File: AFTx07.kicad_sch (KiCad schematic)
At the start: 1 part

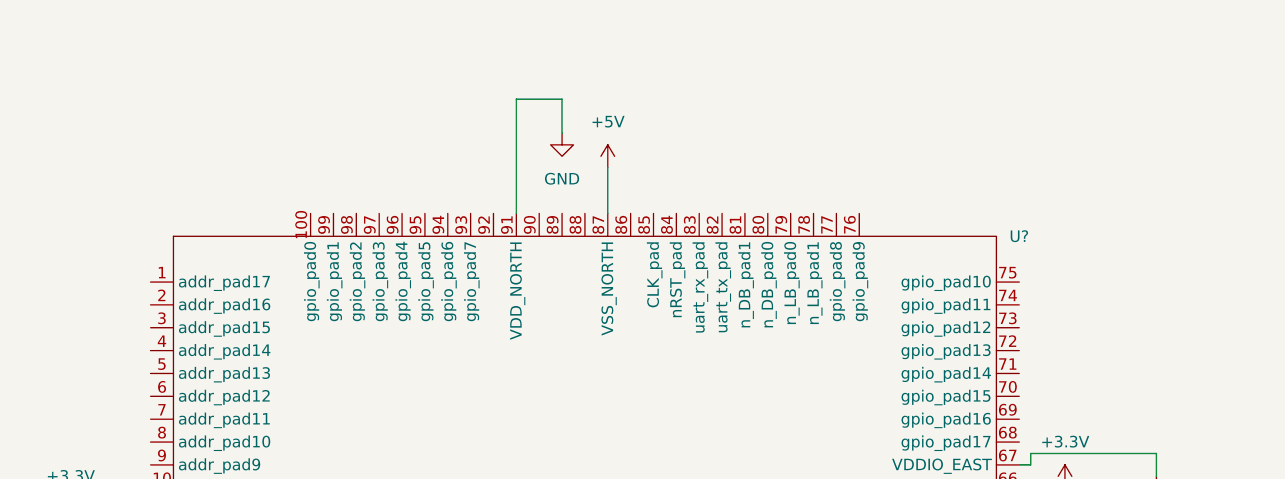
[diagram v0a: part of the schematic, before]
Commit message: Add files via upload
Added sample FMC connector
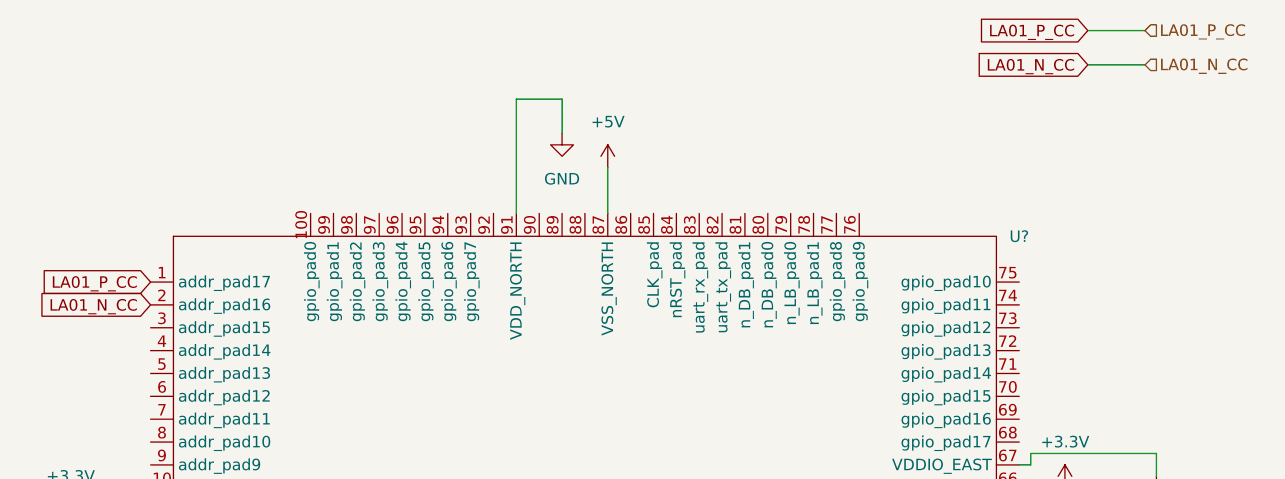
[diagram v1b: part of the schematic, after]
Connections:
- net LA01_P_CC: now reaches U?.1 (addr_pad17)
- net LA01_N_CC: now reaches U?.2 (addr_pad16)
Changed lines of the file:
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@@
+	(wire
+		(pts
+			(xy 180.34 27.94) (xy 186.69 27.94)
+		)
+		(stroke
+			(width 0)
+			(type default)
+		)
+	)
 	(wire
 		(pts
@@
 	(wire
 		(pts
+			(xy 180.34 24.13) (xy 186.69 24.13)
+		)
+		(stroke
+			(width 0)
+			(type default)
+		)
+	)
+	(wire
+		(pts
 			(xy 187.96 73.66) (xy 187.96 71.12)
 		)
@@
 		)
 	)
+	(global_label "LA01_P_CC"
+		(shape input)
+		(at 76.2 52.07 180)
+		(fields_autoplaced yes)
+		(effects
+			(font
+				(size 1.27 1.27)
+			)
+			(justify right)
+		)
+		(property "Intersheetrefs" "${INTERSHEET_REFS}"
+			(at 62.9339 52.07 0)
+			(effects
+				(font
+					(size 1.27 1.27)
+				)
+				(justify right)
+				(hide yes)
+			)
+		)
+	)
+	(global_label "LA01_N_CC"
+		(shape input)
+		(at 180.34 27.94 180)
+		(fields_autoplaced yes)
+		(effects
+			(font
+				(size 1.27 1.27)
+			)
+			(justify right)
+		)
+		(property "Intersheetrefs" "${INTERSHEET_REFS}"
+			(at 167.0134 27.94 0)
+			(effects
+				(font
+					(size 1.27 1.27)
+				)
+				(justify right)
+				(hide yes)
+			)
+		)
+	)
+	(global_label "LA01_P_CC"
+		(shape input)
+		(at 180.34 24.13 180)
+		(fields_autoplaced yes)
+		(effects
+			(font
+				(size 1.27 1.27)
+			)
+			(justify right)
+		)
+		(property "Intersheetrefs" "${INTERSHEET_REFS}"
+			(at 167.0739 24.13 0)
+			(effects
+				(font
+					(size 1.27 1.27)
+				)
+				(justify right)
+				(hide yes)
+			)
+		)
+	)
+	(global_label "LA01_N_CC"
+		(shape input)
+		(at 76.2 54.61 180)
+		(fields_autoplaced yes)
+		(effects
+			(font
+				(size 1.27 1.27)
+			)
+			(justify right)
+		)
+		(property "Intersheetrefs" "${INTERSHEET_REFS}"
+			(at 62.8734 54.61 0)
+			(effects
+				(font
+					(size 1.27 1.27)
+				)
+				(justify right)
+				(hide yes)
+			)
+		)
+	)
+	(hierarchical_label "LA01_P_CC"
+		(shape input)
+		(at 186.69 24.13 0)
+		(fields_autoplaced yes)
+		(effects
+			(font
+				(size 1.27 1.27)
+			)
+			(justify left)
+		)
+	)
+	(hierarchical_label "LA01_N_CC"
+		(shape input)
+		(at 186.69 27.94 0)
+		(fields_autoplaced yes)
+		(effects
+			(font
+				(size 1.27 1.27)
+			)
+			(justify left)
+		)
+	)

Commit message: Add files via upload
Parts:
- gave numbers to parts that had none: 1
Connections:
- net addr8: now reaches U4.10 (addr_pad8)
- net gpio0: now reaches U4.100 (gpio_pad0)
- net addr7: now reaches U4.18 (addr_pad7)
- net addr6: now reaches U4.19 (addr_pad6)
- net addr5: now reaches U4.20 (addr_pad5)
- net addr4: now reaches U4.21 (addr_pad4)
- net addr3: now reaches U4.22 (addr_pad3)
- net addr2: now reaches U4.23 (addr_pad2)
- net addr1: now reaches U4.24 (addr_pad1)
- net addr0: now reaches U4.25 (addr_pad0)
- net nWE1: now reaches U4.26 (n_WE_pad1)
- net nWE0: now reaches U4.27 (n_WE_pad0)
- net nCE0: now reaches U4.28 (n_CE_pad0)
- net nCE1: now reaches U4.29 (n_CE_pad1)
- net addr15: now reaches U4.3 (addr_pad15)
- net nDE1: now reaches U4.30 (n_DE_pad1)
- net nDE0: now reaches U4.31 (n_DE_pad0)
- net data15: now reaches U4.32 (data_pad15)
- net data14: now reaches U4.33 (data_pad14)
- net data13: now reaches U4.34 (data_pad13)
- net data12: now reaches U4.35 (data_pad12)
- net data11: now reaches U4.36 (data_pad11)
- net data10: now reaches U4.37 (data_pad10)
- net data9: now reaches U4.38 (data_pad9)
- net addr14: now reaches U4.4 (addr_pad14)
- net data8: now reaches U4.42 (data_pad8)
- net data7: now reaches U4.43 (data_pad7)
- net data6: now reaches U4.44 (data_pad6)
- net data5: now reaches U4.45 (data_pad5)
- net data4: now reaches U4.46 (data_pad4)
- net data3: now reaches U4.47 (data_pad3)
- net data2: now reaches U4.48 (data_pad2)
- net data1: now reaches U4.49 (data_pad1)
- net addr13: now reaches U4.5 (addr_pad13)
- net data0: now reaches U4.50 (data_pad0)
- net gpio31: now reaches U4.51 (gpio_pad31)
- net gpio30: now reaches U4.52 (gpio_pad30)
- net gpio29: now reaches U4.53 (gpio_pad29)
- net gpio28: now reaches U4.54 (gpio_pad28)
- net gpio27: now reaches U4.55 (gpio_pad27)
- net gpio26: now reaches U4.56 (gpio_pad26)
- net gpio25: now reaches U4.57 (gpio_pad25)
- net gpio24: now reaches U4.58 (gpio_pad24)
- net gpio23: now reaches U4.59 (gpio_pad23)
- net addr12: now reaches U4.6 (addr_pad12)
- net gpio22: now reaches U4.60 (gpio_pad22)
- net gpio21: now reaches U4.61 (gpio_pad21)
- net gpio20: now reaches U4.62 (gpio_pad20)
- net gpio19: now reaches U4.63 (gpio_pad19)
- net gpio18: now reaches U4.64 (gpio_pad18)
- net gpio17: now reaches U4.68 (gpio_pad17)
- net gpio16: now reaches U4.69 (gpio_pad16)
- net addr11: now reaches U4.7 (addr_pad11)
- net gpio15: now reaches U4.70 (gpio_pad15)
- net gpio14: now reaches U4.71 (gpio_pad14)
- net gpio13: now reaches U4.72 (gpio_pad13)
- net gpio12: now reaches U4.73 (gpio_pad12)
- net gpio11: now reaches U4.74 (gpio_pad11)
- net gpio10: now reaches U4.75 (gpio_pad10)
- net gpio9: now reaches U4.76 (gpio_pad9)
- net gpio8: now reaches U4.77 (gpio_pad8)
- net nLB1: now reaches U4.78 (n_LB_pad1)
- net nLB0: now reaches U4.79 (n_LB_pad0)
- net addr10: now reaches U4.8 (addr_pad10)
- net nDB0: now reaches U4.80 (n_DB_pad0)
- net nDB1: now reaches U4.81 (n_DB_pad1)
- net uart.tx: now reaches U4.82 (uart_tx_pad)
- net uart.rx: now reaches U4.83 (uart_rx_pad)
- net nRST: now reaches U4.84 (nRST_pad)
- net CLK: now reaches U4.85 (CLK_pad)
- net addr9: now reaches U4.9 (addr_pad9)
- net gpio7: now reaches U4.93 (gpio_pad7)
- net gpio6: now reaches U4.94 (gpio_pad6)
- net gpio5: now reaches U4.95 (gpio_pad5)
- net gpio4: now reaches U4.96 (gpio_pad4)
- net gpio3: now reaches U4.97 (gpio_pad3)
- net gpio2: now reaches U4.98 (gpio_pad2)
- net gpio1: now reaches U4.99 (gpio_pad1)
- net LA01_N_CC renamed addr16
- net LA01_P_CC renamed addr17

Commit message: Add files via upload
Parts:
- renumbered U4 to U?
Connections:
- net addr0: no longer names the net of U?.25 (addr_pad0)
- net addr1: no longer names the net of U?.24 (addr_pad1)
- net addr10: no longer names the net of U?.8 (addr_pad10)
- net addr11: no longer names the net of U?.7 (addr_pad11)
- net addr12: no longer names the net of U?.6 (addr_pad12)
- net addr13: no longer names the net of U?.5 (addr_pad13)
- net addr14: no longer names the net of U?.4 (addr_pad14)
- net addr15: no longer names the net of U?.3 (addr_pad15)
- net addr16 renamed LA01_N_CC
- net addr17 renamed LA01_P_CC
- net addr2: no longer names the net of U?.23 (addr_pad2)
- net addr3: no longer names the net of U?.22 (addr_pad3)
- net addr4: no longer names the net of U?.21 (addr_pad4)
- net addr5: no longer names the net of U?.20 (addr_pad5)
- net addr6: no longer names the net of U?.19 (addr_pad6)
- net addr7: no longer names the net of U?.18 (addr_pad7)
- net addr8: no longer names the net of U?.10 (addr_pad8)
- net addr9: no longer names the net of U?.9 (addr_pad9)
- net data0: no longer names the net of U?.50 (data_pad0)
- net data1: no longer names the net of U?.49 (data_pad1)
- net data10: no longer names the net of U?.37 (data_pad10)
- net data11: no longer names the net of U?.36 (data_pad11)
- net data12: no longer names the net of U?.35 (data_pad12)
- net data13: no longer names the net of U?.34 (data_pad13)
- net data14: no longer names the net of U?.33 (data_pad14)
- net data15: no longer names the net of U?.32 (data_pad15)
- net data2: no longer names the net of U?.48 (data_pad2)
- net data3: no longer names the net of U?.47 (data_pad3)
- net data4: no longer names the net of U?.46 (data_pad4)
- net data5: no longer names the net of U?.45 (data_pad5)
- net data6: no longer names the net of U?.44 (data_pad6)
- net data7: no longer names the net of U?.43 (data_pad7)
- net data8: no longer names the net of U?.42 (data_pad8)
- net data9: no longer names the net of U?.38 (data_pad9)
- net gpio0: no longer names the net of U?.100 (gpio_pad0)
- net gpio1: no longer names the net of U?.99 (gpio_pad1)
- net gpio10: no longer names the net of U?.75 (gpio_pad10)
- net gpio11: no longer names the net of U?.74 (gpio_pad11)
- net gpio12: no longer names the net of U?.73 (gpio_pad12)
- net gpio13: no longer names the net of U?.72 (gpio_pad13)
- net gpio14: no longer names the net of U?.71 (gpio_pad14)
- net gpio15: no longer names the net of U?.70 (gpio_pad15)
- net gpio16: no longer names the net of U?.69 (gpio_pad16)
- net gpio17: no longer names the net of U?.68 (gpio_pad17)
- net gpio18: no longer names the net of U?.64 (gpio_pad18)
- net gpio19: no longer names the net of U?.63 (gpio_pad19)
- net gpio2: no longer names the net of U?.98 (gpio_pad2)
- net gpio20: no longer names the net of U?.62 (gpio_pad20)
- net gpio21: no longer names the net of U?.61 (gpio_pad21)
- net gpio22: no longer names the net of U?.60 (gpio_pad22)
- net gpio23: no longer names the net of U?.59 (gpio_pad23)
- net gpio24: no longer names the net of U?.58 (gpio_pad24)
- net gpio25: no longer names the net of U?.57 (gpio_pad25)
- net gpio26: no longer names the net of U?.56 (gpio_pad26)
- net gpio27: no longer names the net of U?.55 (gpio_pad27)
- net gpio28: no longer names the net of U?.54 (gpio_pad28)
- net gpio29: no longer names the net of U?.53 (gpio_pad29)
- net gpio3: no longer names the net of U?.97 (gpio_pad3)
- net gpio30: no longer names the net of U?.52 (gpio_pad30)
- net gpio31: no longer names the net of U?.51 (gpio_pad31)
- net gpio4: no longer names the net of U?.96 (gpio_pad4)
- net gpio5: no longer names the net of U?.95 (gpio_pad5)
- net gpio6: no longer names the net of U?.94 (gpio_pad6)
- net gpio7: no longer names the net of U?.93 (gpio_pad7)
- net gpio8: no longer names the net of U?.77 (gpio_pad8)
- net gpio9: no longer names the net of U?.76 (gpio_pad9)
- net nCE0: no longer names the net of U?.28 (n_CE_pad0)
- net nCE1: no longer names the net of U?.29 (n_CE_pad1)
- net nDB0: no longer names the net of U?.80 (n_DB_pad0)
- net nDB1: no longer names the net of U?.81 (n_DB_pad1)
- net nDE0: no longer names the net of U?.31 (n_DE_pad0)
- net nDE1: no longer names the net of U?.30 (n_DE_pad1)
- net nLB0: no longer names the net of U?.79 (n_LB_pad0)
- net nLB1: no longer names the net of U?.78 (n_LB_pad1)
- net nRST: no longer names the net of U?.84 (nRST_pad)
- net nWE0: no longer names the net of U?.27 (n_WE_pad0)
- net nWE1: no longer names the net of U?.26 (n_WE_pad1)
- net uart.rx: no longer names the net of U?.83 (uart_rx_pad)
- net uart.tx: no longer names the net of U?.82 (uart_tx_pad)
